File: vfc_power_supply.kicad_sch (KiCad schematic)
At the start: 21 parts, among them J1 Conn_01x03_Male, J2 Conn_01x03_Male, J3 Conn_01x02_Male, J4 Raspberry_Pi_4B, M1 Logo_10mmx10mm

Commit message: Mostly complete, just missing a few tracks and review
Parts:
- removed FL1: EMI_Filter_CommonMode, Inductor_WUT:TDK_ACM7060-301-2PL-TL01, symbol Device:EMI_Filter_CommonMode
- removed J2: Conn_01x03_Male, Connector_WUT:Powerpole_PP30-with-1377G2-PCB-pins-25A_3WAY, symbol Connector:Conn_01x03_Male
- added J2: Conn_01x06_Female, Connector_WUT:Weidmuller_SL3.5-6-90G, symbol Connector:Conn_01x06_Female
- added R5, R6, R7, R8, R9: 100, Resistor_SMD:R_0603_1608Metric, symbol Device:R
- R1, R2: footprint Resistor_SMD:R_0402_1005Metric -> Resistor_SMD:R_0603_1608Metric
- R10: renamed from R5; footprint Resistor_SMD:R_0402_1005Metric -> Resistor_SMD:R_0603_1608Metric
- R11: renamed from R6; footprint Resistor_SMD:R_0402_1005Metric -> Resistor_SMD:R_0603_1608Metric
- R12: renamed from R7; footprint Resistor_SMD:R_0402_1005Metric -> Resistor_SMD:R_0603_1608Metric
- R13: renamed from R8; footprint Resistor_SMD:R_0402_1005Metric -> Resistor_SMD:R_0603_1608Metric
- R14: renamed from R9; footprint Resistor_SMD:R_0402_1005Metric -> Resistor_SMD:R_0603_1608Metric
- R15: renamed from R10; footprint Resistor_SMD:R_0402_1005Metric -> Resistor_SMD:R_0603_1608Metric
- R16: renamed from R11; footprint Resistor_SMD:R_0402_1005Metric -> Resistor_SMD:R_0603_1608Metric
- R3: renamed from R4; footprint Resistor_SMD:R_0402_1005Metric -> Resistor_SMD:R_0603_1608Metric
- R4: renamed from R3; footprint Resistor_SMD:R_0402_1005Metric -> Resistor_SMD:R_0603_1608Metric
- renumbered FL2 to FL1
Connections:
- net ADC/CH0: now also R2.2; no longer R1.2
- net ADC/CH1: now also R1.2; no longer R2.2
- net ADC/CH2: now also R3.2; no longer R4.2
- net ADC/CH3: now also R4.2; no longer R3.2
- net GND: now also FL1.4, J2.6 (Pin_6); no longer FL1.3
- net Network Switch Load Switch/VOUT: now also FL1.2; no longer FL1.1
- net PGOOD_5V: now also J4.22 (GPIO25/~SPI4_CS1~); no longer J4.8 (GPIO14/TXD0/SPI5_MOSI/TXD1)
- net PGOOD_POE: now also J4.40 (GPIO21/SPI6_SCLK/SPI1_SCLK); no longer J4.31 (GPIO6/SPI4_MOSI/SDA4)
- net PGOOD_SWITCH: now also J4.32 (GPIO12/~SPI5_CS0~/TXD5/SDA5); no longer J4.23 (GPIO11/SPI0_SCLK/SCL5)
- net RGB_BLUE: now also J4.15 (GPIO22/SDA6); no longer J4.11 (GPIO17/~SPI1_CS1~)
- net RGB_RED: now also J4.11 (GPIO17/~SPI1_CS1~); no longer J4.15 (GPIO22/SDA6)
- net ~EN_POE: now also J4.38 (GPIO20/SPI6_MOSI/SPI1_MOSI); no longer J4.33 (GPIO13/SPI5_MISO/RXD5/SCL5)
- net ~FAULT_POE: now also J4.36 (GPIO16/~SPI1_CS2~); no longer J4.35 (GPIO19/SPI6_MISO/SPI1_MISO)
- net ~FAULT_SWITCH: now also J4.24 (GPIO8/~SPI0_CS0~/TXD4/SDA4); no longer J4.29 (GPIO5/SPI4_MISO/RXD3/SCL3)
- net at C1.1, J3.1 (Pin_1): now also FL1.1; no longer FL1.2
- net at C1.2, J3.2 (Pin_2): now also FL1.3; no longer FL1.4
- net GPIO15/RXD: now reaches J4.10 (GPIO15/RXD0/SPI5_SCLK/RXD1)
- net GPIO15/RXD: now also R7.1
- net GPIO10/SDA: now reaches J4.19 (GPIO10/SPI0_MOSI/SDA5)
- net GPIO10/SDA: now also R6.1
- net GPIO9/SCL: now reaches J4.21 (GPIO9/SPI0_MISO/RXD4/SCL4)
- net GPIO9/SCL: now also R5.1
- net OPTO_OUT_0: now reaches J4.37 (GPIO26/~SPI5_CS0~)
- net GPIO4/ONE_WIRE: now reaches J4.7 (GPIO4/~SPI4_CS0~/TXD3/SDA3)
- net GPIO4/ONE_WIRE: now also R9.1
- new net: J2.1 (Pin_1), R5.2
- new net: J2.2 (Pin_2), R6.2
- new net: J2.3 (Pin_3), R7.2
- new net: J2.4 (Pin_4), R8.2
- new net: J2.5 (Pin_5), R9.2
- new net GPIO14/TXD: J4.8 (GPIO14/TXD0/SPI5_MOSI/TXD1), R8.1
- new net OPTO_IN_0: J4.31 (GPIO6/SPI4_MOSI/SDA4)
- new net OPTO_IN_1: J4.29 (GPIO5/SPI4_MISO/RXD3/SCL3)
- new net OPTO_IN_2: J4.23 (GPIO11/SPI0_SCLK/SCL5)
- new net OPTO_OUT_1: J4.35 (GPIO19/SPI6_MISO/SPI1_MISO)
- new net OPTO_OUT_2: J4.33 (GPIO13/SPI5_MISO/RXD5/SCL5)
- no-connect marks 17 -> 5
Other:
- added sheet Optoisolators (optoisolators.kicad_sch)
- sheet ADC ports: added none; removed 0V_SENSE, VBAT_SENSE
- note removed: "GPIO10"
- note removed: "GPIO11"
- note removed: "GPIO13"
- note removed: "GPIO17"
- note removed: "GPIO19"
- note removed: "GPIO2"
- note removed: "GPIO22"
- note removed: "GPIO26"
- note removed: "GPIO27"
- note removed: "GPIO3"
- note removed: "GPIO4"
- note removed: "GPIO5"
- note removed: "GPIO6"
- note removed: "GPIO9"
- note removed: "Isolated sense channel for battery voltage without voltage drop in main supply"
- moved on the sheet: R3, R4

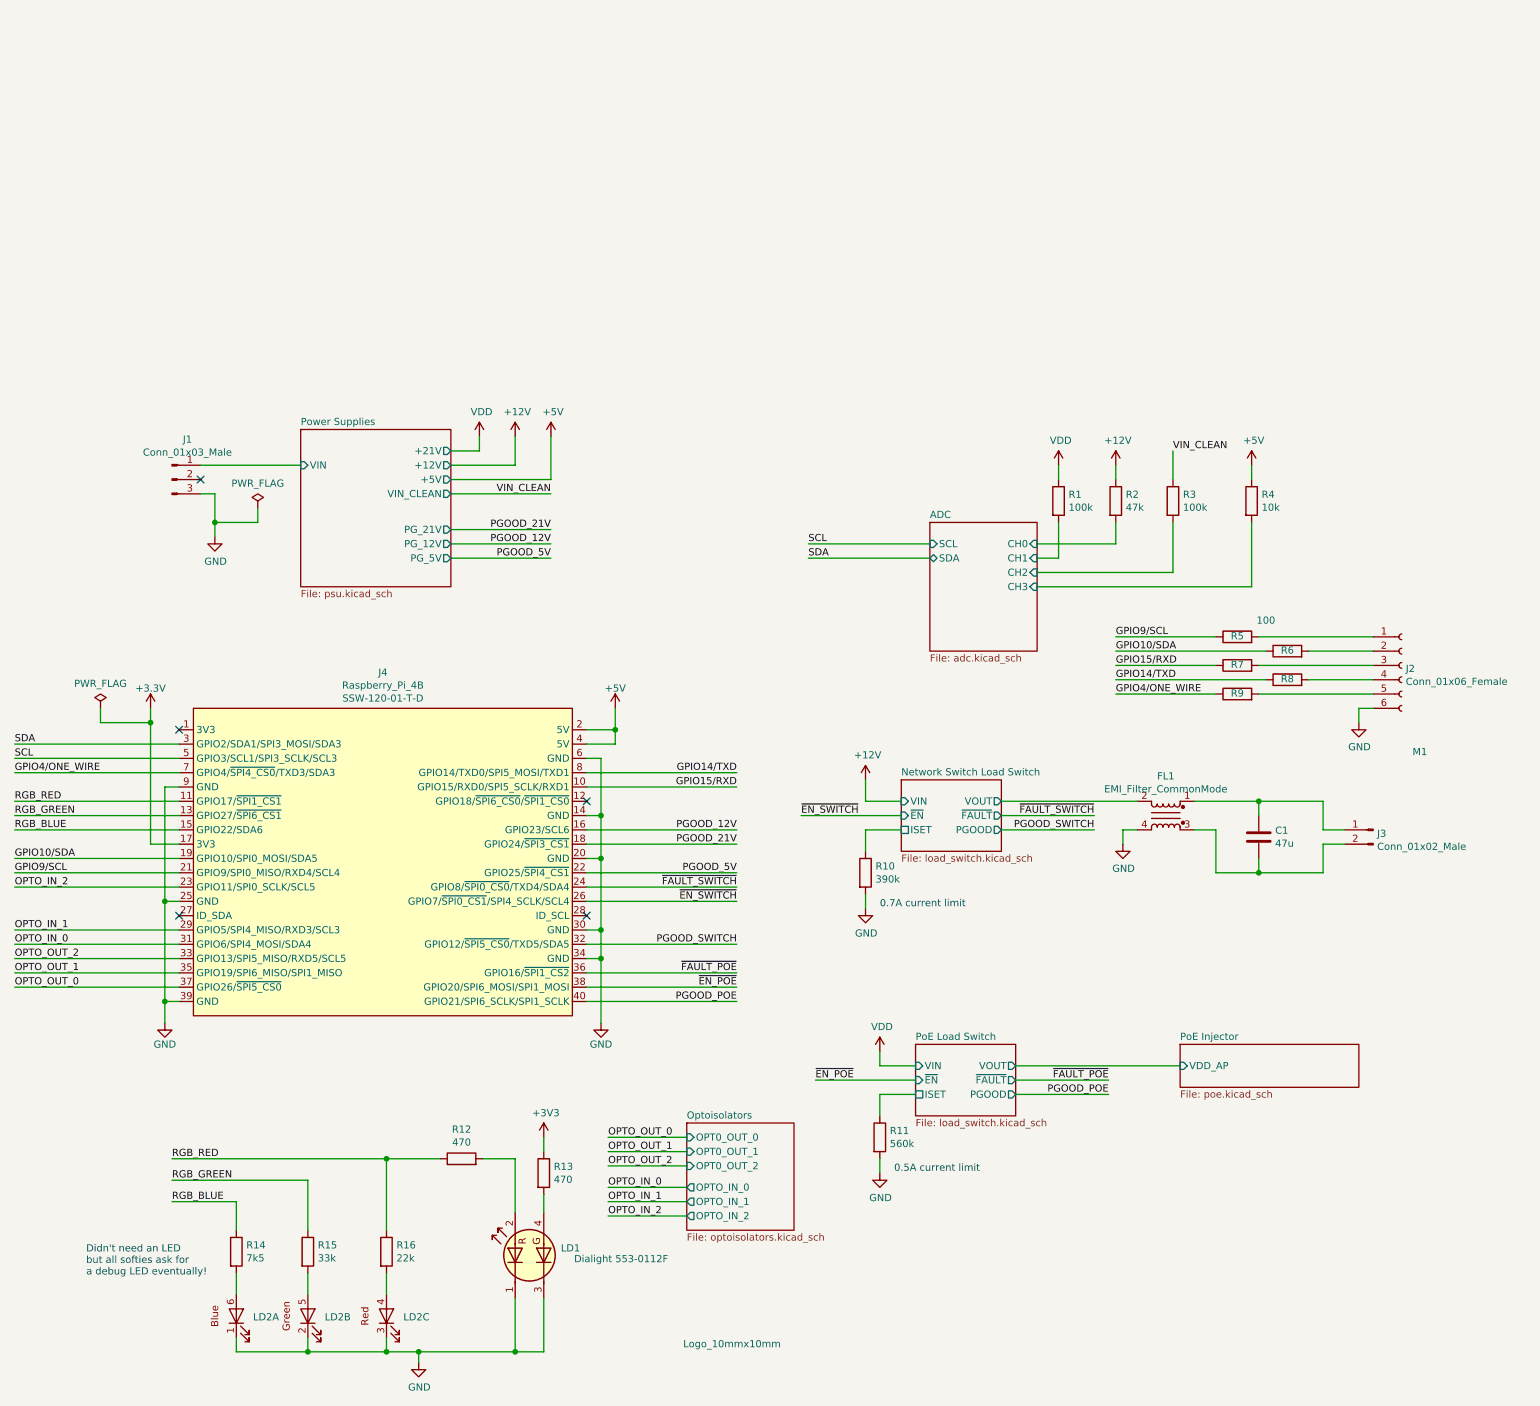
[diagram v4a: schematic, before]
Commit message: Finished tidying up silkscreen
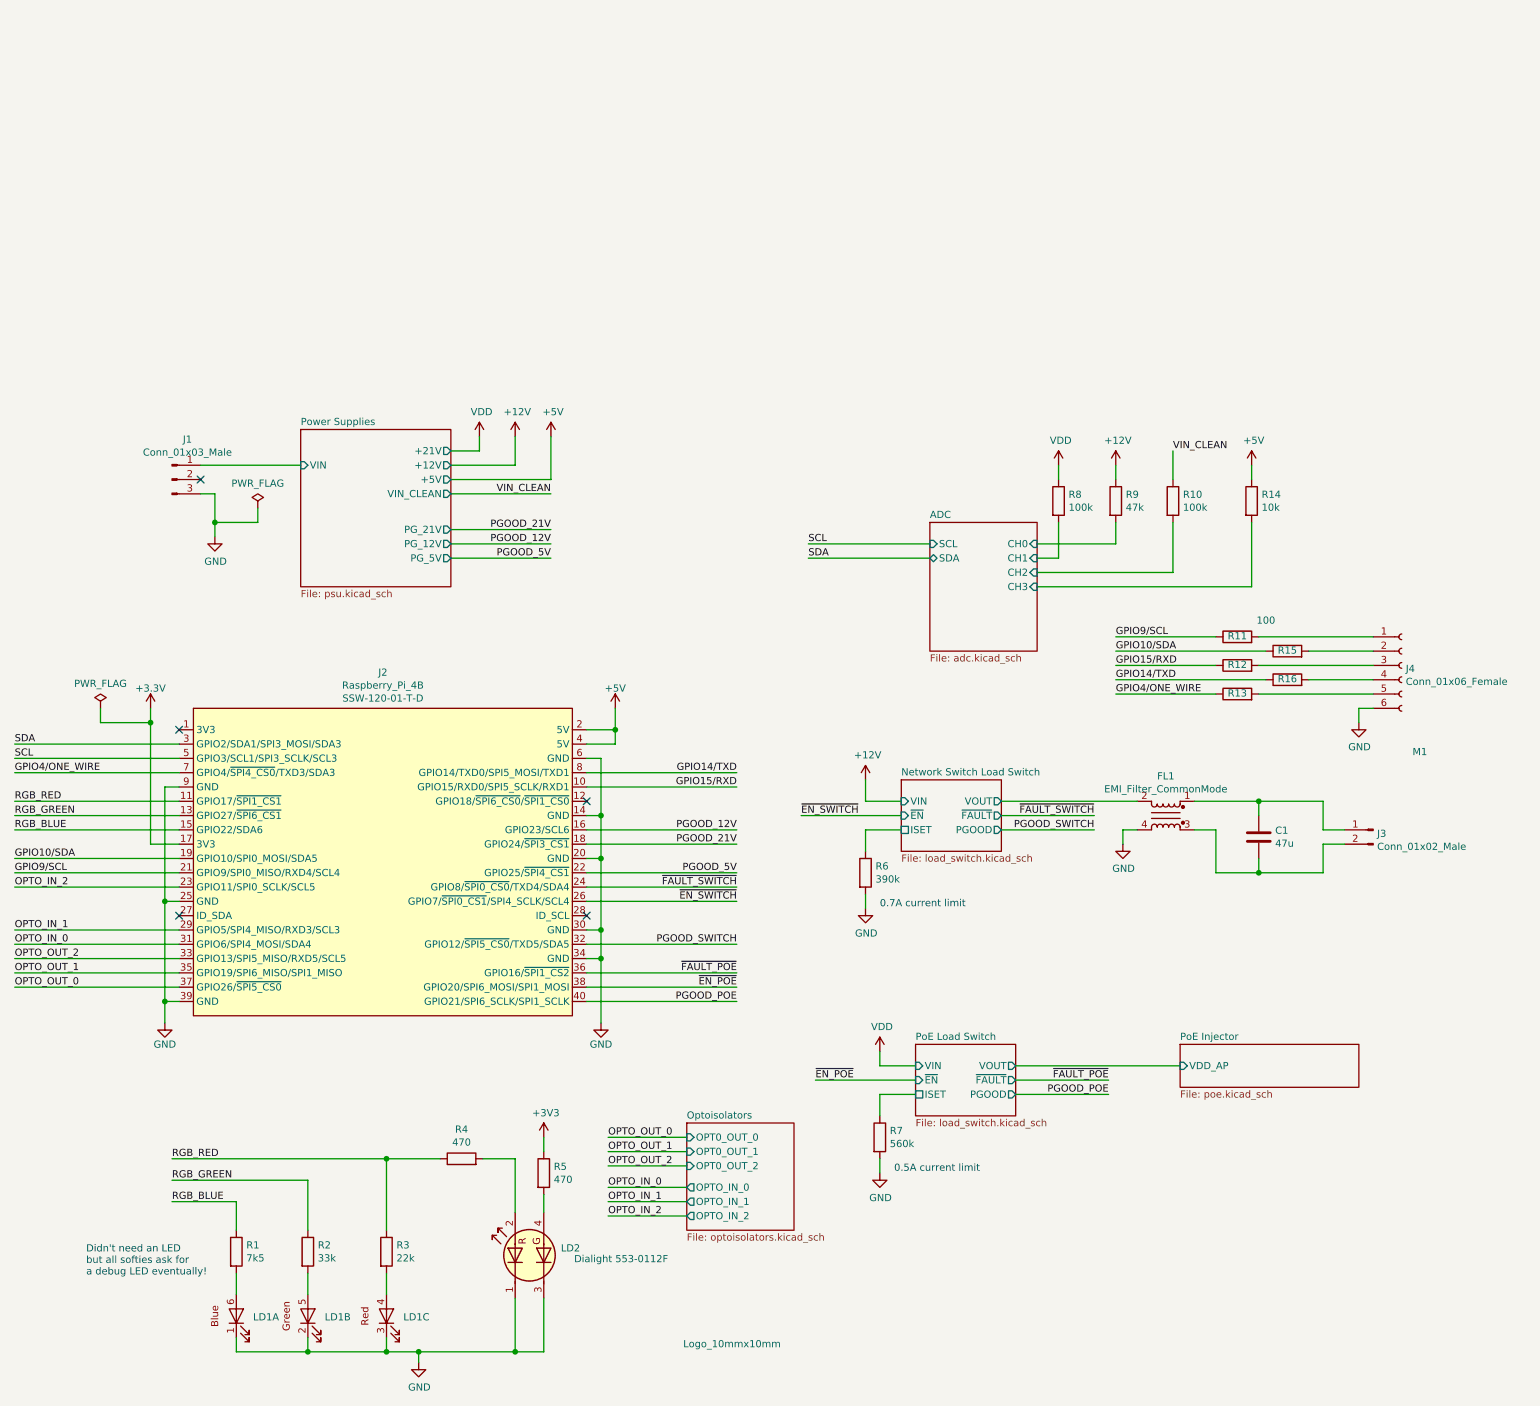
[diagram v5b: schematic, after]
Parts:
- renumbered J4 to J2, J2 to J4, LD2 to LD1, LD1 to LD2, R14 to R1, R3 to R10, R5 to R11, R7 to R12, R9 to R13, R4 to R14, R6 to R15, R8 to R16, R15 to R2, R16 to R3, R12 to R4, R13 to R5, R10 to R6, R11 to R7, R1 to R8, R2 to R9

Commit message: Added changes following review from RMC
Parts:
- added R60, R61: 100, Resistor_SMD:R_0402_1005Metric, symbol Device:R
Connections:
- net +3V3: now also J2.1 (3V3)
- net ~EN_POE: now also R61.1
- net ~EN_SWITCH: now also R60.1
- new net Network Switch Load Switch/~EN: R60.2
- new net PoE Load Switch/~EN: R61.2
- no-connect marks 5 -> 4
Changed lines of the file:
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@@
   )
   (junction (at 43.18 72.39) (diameter 1.016) (color 0 0 0 0))
+  (junction (at 43.18 73.66) (diameter 1.016) (color 0 0 0 0))
   (junction (at 45.72 104.14) (diameter 1.016) (color 0 0 0 0))
   (junction (at 45.72 121.92) (diameter 1.016) (color 0 0 0 0))
@@
   (junction (at 240.03 86.36) (diameter 1.016) (color 0 0 0 0))
   (junction (at 240.03 99.06) (diameter 1.016) (color 0 0 0 0))
-  (no_connect (at 48.26 73.66))
   (no_connect (at 48.26 106.68))
   (no_connect (at 52.07 29.21))
@@
     (stroke (width 0) (type solid) (color 0 0 0 0))
   )
-  (wire (pts (xy 43.18 72.39) (xy 43.18 93.98))
+  (wire (pts (xy 43.18 72.39) (xy 43.18 73.66))
+    (stroke (width 0) (type solid) (color 0 0 0 0))
+  )
+  (wire (pts (xy 43.18 73.66) (xy 43.18 93.98))
+    (stroke (width 0) (type solid) (color 0 0 0 0))
+  )
+  (wire (pts (xy 43.18 73.66) (xy 48.26 73.66))
     (stroke (width 0) (type solid) (color 0 0 0 0))
   )
@@
     (stroke (width 0) (type solid) (color 0 0 0 0))
   )
-  (wire (pts (xy 158.75 88.9) (xy 176.53 88.9))
+  (wire (pts (xy 149.86 88.9) (xy 161.29 88.9))
+    (stroke (width 0) (type solid) (color 0 0 0 0))
+  )
+  (wire (pts (xy 152.4 135.89) (xy 161.29 135.89))
     (stroke (width 0) (type solid) (color 0 0 0 0))
   )
@@
     (stroke (width 0) (type solid) (color 0 0 0 0))
   )
-  (wire (pts (xy 161.29 135.89) (xy 179.07 135.89))
+  (wire (pts (xy 168.91 88.9) (xy 176.53 88.9))
+    (stroke (width 0) (type solid) (color 0 0 0 0))
+  )
+  (wire (pts (xy 168.91 135.89) (xy 179.07 135.89))
     (stroke (width 0) (type solid) (color 0 0 0 0))
   )
@@
     (effects (font (size 1.27 1.27)) (justify right bottom))
   )
-  (label "~EN_SWITCH" (at 158.75 88.9 0)
+  (label "~EN_SWITCH" (at 149.86 88.9 0)
+    (effects (font (size 1.27 1.27)) (justify left bottom))
+  )
+  (label "~EN_POE" (at 152.4 135.89 0)
     (effects (font (size 1.27 1.27)) (justify left bottom))
   )
@@
   )
   (label "SDA" (at 160.02 43.18 0)
-    (effects (font (size 1.27 1.27)) (justify left bottom))
-  )
-  (label "~EN_POE" (at 161.29 135.89 0)
     (effects (font (size 1.27 1.27)) (justify left bottom))
   )
@@
     )
     (property "Datasheet" "~" (id 3) (at 113.03 152.4 0)
+      (effects (font (size 1.27 1.27)) hide)
+    )
+  )
+  (symbol (lib_id "Device:R") (at 165.1 88.9 90) (unit 1)
+    (in_bom yes) (on_board yes)
+    (property "Reference" "R60" (id 0) (at 165.1 83.6738 90))
+    (property "Value" "100" (id 1) (at 165.1 85.972 90))
+    (property "Footprint" "Resistor_SMD:R_0402_1005Metric" (id 2) (at 165.1 90.678 90)
+      (effects (font (size 1.27 1.27)) hide)
+    )
+    (property "Datasheet" "~" (id 3) (at 165.1 88.9 0)
+      (effects (font (size 1.27 1.27)) hide)
+    )
+  )
+  (symbol (lib_id "Device:R") (at 165.1 135.89 90) (unit 1)
+    (in_bom yes) (on_board yes)
+    (property "Reference" "R61" (id 0) (at 165.1 130.6638 90))
+    (property "Value" "100" (id 1) (at 165.1 132.962 90))
+    (property "Footprint" "Resistor_SMD:R_0402_1005Metric" (id 2) (at 165.1 137.668 90)
+      (effects (font (size 1.27 1.27)) hide)
+    )
+    (property "Datasheet" "~" (id 3) (at 165.1 135.89 0)
       (effects (font (size 1.27 1.27)) hide)
     )
@@
       (reference "R16") (unit 1) (value "100") (footprint "Resistor_SMD:R_0603_1608Metric")
     )
+    (path "/be11ed4f-3726-4fd0-ae3f-7b63712675ce"
+      (reference "R60") (unit 1) (value "100") (footprint "Resistor_SMD:R_0402_1005Metric")
+    )
+    (path "/9579b5b3-c213-498b-850b-25fe82959a39"
+      (reference "R61") (unit 1) (value "100") (footprint "Resistor_SMD:R_0402_1005Metric")
+    )
     (path "/00000000-0000-0000-0000-00005fcc0c15/00000000-0000-0000-0000-00006020d38f"
